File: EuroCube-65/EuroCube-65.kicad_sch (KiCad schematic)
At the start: 102 parts, among them CON1 SERIAL PORT, CON2 PARALLEL PORT, CON3 EXPANSION BUS, IC1 6551A, IC10 GAL16V8, IC11 6522, IC12 6502, IC13 7660, IC2 26LS30, IC3 M3002, IC4 26LS32, IC5 74LS04, IC7 74LS00, IC8 74HCT132, IC9 GAL16V8, T1 BC547, T2 2N7000, T3 2N3906, X1 1.843MHz, X2 32.768kHz, X3 1MHz

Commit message: Updated typo, added bom/ibom
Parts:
- B1: Source (none) -> NiMh: https://www.ebay.com/itm/303608055779 or Coin cell: h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
- C1, C15, C17, C18, C19, C27, C4, C6, C7, C9: Source (none) -> Mouser https://mou.sr/3VUTNs3
- C10, C11, C12, C13: Source (none) -> Mouser https://mou.sr/4iUAKb8
- C16: Source (none) -> Mouser https://mou.sr/4iWQR84
- C20, C30: Source (none) -> Mouser https://mou.sr/3O75zLF
- C21, C22, C28, C29: Source (none) -> Use 13pF matched to crystals linked below, Mouser https://m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
- C23: Source (none) -> Mouser https://mou.sr/3DLIpZ6
- C24, C25: Source (none) -> Mouser https://mou.sr/3BQdcDy
- C8: Source (none) -> (or 5-30pF) must be small footprint e.g. Anchor Electronics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
- CON1: Source (none) -> DIN-7 ebay example: https://www.ebay.com/itm/254570069647
- CON2: Source (none) -> 26W Latching RA header, male, long latches, Anchor Electron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
- CON3: Source (none) -> DIN 41612, 2 row, 64 pos, male, RA, Mouser https://mou.sr/4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
- D1, D2, D4: Source (none) -> Mouser https://mou.sr/3wZtszk (plus one extra if using a co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
- D3: Source (none) -> Mouser https://mou.sr/4fJod7r
- IC1: Source (none) -> Ebay, example: https://www.ebay.com/itm/254521312074
- IC10, IC9: Source (none) -> Ebay, example: https://www.ebay.com/itm/363965912636
- IC11: Source (none) -> Ebay, example: https://www.ebay.com/itm/145848493201
- IC12: Source (none) -> Ebay, example: https://www.ebay.com/itm/405284509359
- IC13: Source (none) -> Mouser https://mou.sr/4iOD8jP
- IC2, X2: Source (none) -> Anchor Electronics https://anchor-electronics.com/price-lis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
- IC3: Source (none) -> Ebay, example: https://www.ebay.com/itm/226476043911
- IC4: Source (none) -> Mouser https://mou.sr/420G8TU
- IC5: Source (none) -> Mouser https://mou.sr/3TKMrV4
- IC7: Source (none) -> Mouser https://mou.sr/3w5Mdxk
- IC8: Source (none) -> Mouser https://mou.sr/4gUzrHh
- L10: Source (none) -> 0.1" pin header
- L2, L3, L4, L5, L6, L7, L8, L9, M0, M1, M2, M3, S1, S2, S3, S4: Source (none) -> 0.1" pin headers / for S2 use https://www.digikey.com/short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
- R10, R11, R12, R13: Source (none) -> Mouser https://mou.sr/3S4nkwA
- R14, R9: Source (none) -> Mouser https://mou.sr/4gSpnyA
- R15, R16: Source (none) -> Mouser https://mou.sr/3BFqHWN
- R17: Source (none) -> Mouser https://mou.sr/4gAKzt4
- R18, R31: Source (none) -> Mouser https://mou.sr/4gzF7GX
- R19, R5: Source (none) -> Mouser https://mou.sr/3DDC2XZ
- R2: Source (none) -> Mouser https://mou.sr/40g8pVm
- R23, R24, R25, R27, R28: Source (none) -> Mouser https://mou.sr/4gFZO4k
- R26, R3, R4: Source (none) -> Mouser https://mou.sr/4fHA8mv
- R29, R30: Source (none) -> Mouser https://mou.sr/4j0kbdN
- R6: Source (none) -> Mouser https://mou.sr/3PjO638
- R7: Source (none) -> e.g. 470R Mouser https://mou.sr/3PjO638
- R8: Source (none) -> Mouser https://mou.sr/3BGw6gi
- RP1: Source (none) -> Mouser https://mou.sr/4fGkWG9
- T1: Source (none) -> Mouser https://mou.sr/3Dz5VIR
- T2: Source (none) -> Mouser https://mou.sr/47xjkvW
- T3: Source (none) -> Mouser https://mou.sr/4gzFu4j
- X1: Source (none) -> Mouser https://mou.sr/3PeAg1M
- X3: Source (none) -> Mouser https://mou.sr/3PdVQDI
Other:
- note added: "M3/M2"
- note added: "Notes: 1. Fit C10-13 to slew-rate limit serial outputs (not normally needed) 2. Fit R9,R14 for RS-422 terminating resistors (not needed for RS-232/423) 3. R31, BUSY+(RTS) pull-up resistor added to avoid BBC modification (see manual P51) 4. Fit L2,L3 by default for RS-232/423 operation / remove for RS-422 network 5. Fit L3 (pos 3-4) by default for RS-232/423 with on-board -5V supply (IC13) 6. Fit 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"
- note removed: "Notes: 1. Fit C10-13 to slew-rate limit serial outputs (not normally needed) 2. Fit R9,R14 for RS-422 terminating resistors (not needed for RS-232/423 3. R31, BUSY+(RTS) pull-up resistor added to avoid BBC modification (see manual P51) 4. Fit L2,L3 by default for RS-232/423 operation / remove for RS-422 network 5. Fit L3 (pos 3-4) by default for RS-232/423 with on-board -5V supply (IC13) 6. Fit L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"

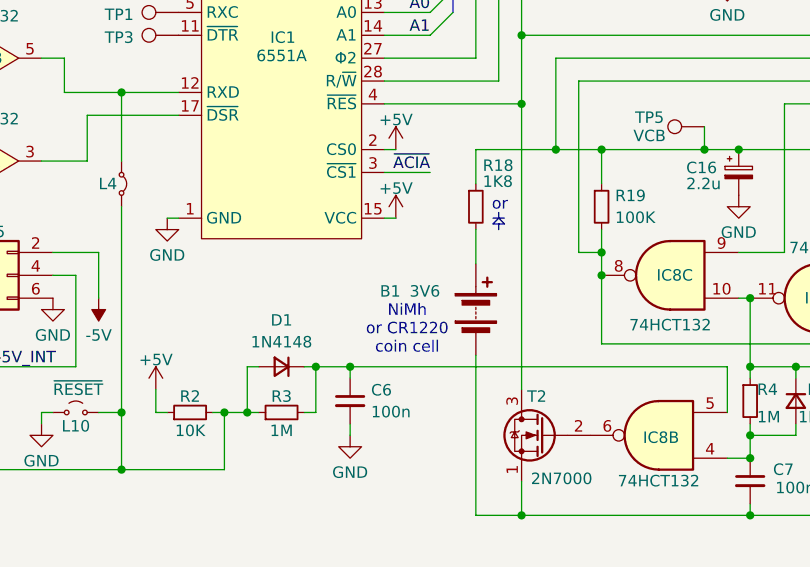
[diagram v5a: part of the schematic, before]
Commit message: Updated BOM with correct battery references
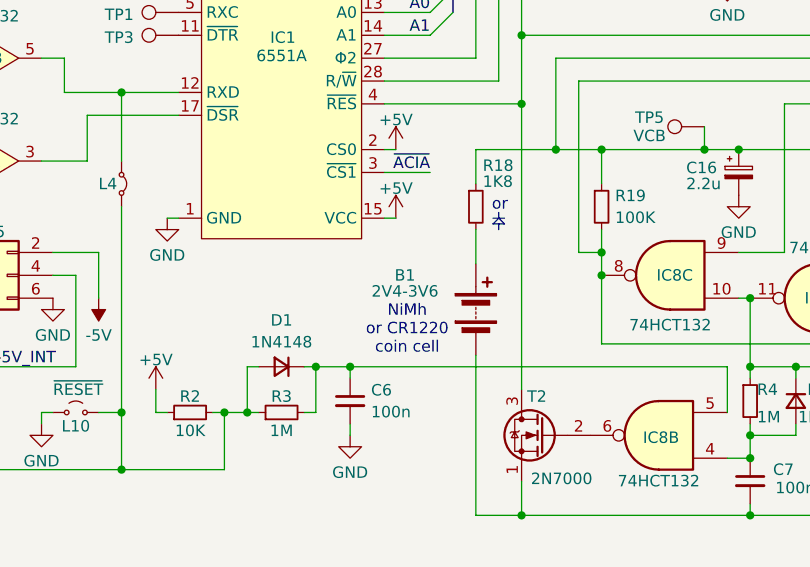
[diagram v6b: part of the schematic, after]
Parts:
- B1: value 3V6 -> 2V4-3V6; Source NiMh: https://www.ebay.com/itm/303608055779 or Coin cell: h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 -> NiMh: https://www.ebay.com/itm/303608055779 or CR1220 coin 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
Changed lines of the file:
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@@
 		(dnp no)
 		(property "Reference" "B1"
-			(at 154.432 218.948 0)
+			(at 157.226 217.17 0)
 			(effects
 				(font
 					(size 1.27 1.27)
 				)
-				(justify left)
 			)
 		)
-		(property "Value" "3V6"
-			(at 157.734 218.948 0)
+		(property "Value" "2V4-3V6"
+			(at 157.226 218.948 0)
 			(effects
 				(font
 					(size 1.27 1.27)
 				)
-				(justify left)
 			)
 		)
@@
 			)
 		)
-		(property "Source" "NiMh: https://www.ebay.com/itm/303608055779 or Coin cell: https://mou.sr/4iOCzqd "
+		(property "Source" "NiMh: https://www.ebay.com/itm/303608055779 or CR1220 coin cell (https://a.co/d/0sKtg3F) and holder (https://mou.sr/4iOCzqd)"
 			(at 165.1 220.98 0)
 			(effects
